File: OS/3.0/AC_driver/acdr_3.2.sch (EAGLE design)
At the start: 61 parts, among them T1 BT1308W, T2 MAC97SOT223, T3 MAC97SOT223, T4 MAC97SOT223, T5 MAC97SOT223, T6 MAC97SOT223, T7 MAC97SOT223, T8 MAC97SOT223

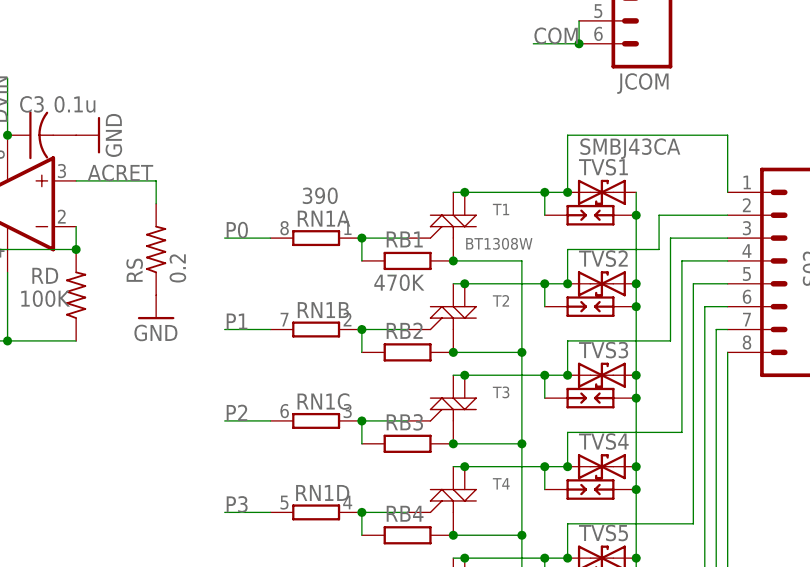
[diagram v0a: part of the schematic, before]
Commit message: correct the pull down resistor value
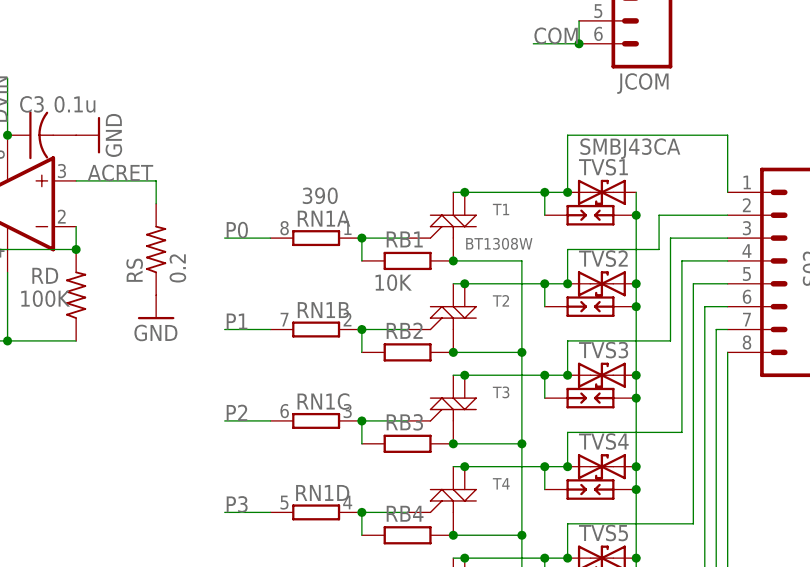
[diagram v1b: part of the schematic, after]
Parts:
- RB1, RB2, RB3, RB4, RB5, RB6, RB7, RB8: value 470K -> 10K
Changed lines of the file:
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@@
 <?xml version="1.0" encoding="utf-8"?>
 <!DOCTYPE eagle SYSTEM "eagle.dtd">
-<eagle version="9.3.0">
+<eagle version="9.6.2">
 <drawing>
 <settings>
@@
 <part name="SP7" library="varistor" deviceset="PCB-SGAP" device="" value="PCB-SGAP"/>
 <part name="SP8" library="varistor" deviceset="PCB-SGAP" device="" value="PCB-SGAP"/>
-<part name="RB1" library="rcl" deviceset="R-EU_" device="R0603" value="470K"/>
-<part name="RB2" library="rcl" deviceset="R-EU_" device="R0603" value="470K"/>
-<part name="RB3" library="rcl" deviceset="R-EU_" device="R0603" value="470K"/>
-<part name="RB4" library="rcl" deviceset="R-EU_" device="R0603" value="470K"/>
-<part name="RB5" library="rcl" deviceset="R-EU_" device="R0603" value="470K"/>
-<part name="RB6" library="rcl" deviceset="R-EU_" device="R0603" value="470K"/>
-<part name="RB7" library="rcl" deviceset="R-EU_" device="R0603" value="470K"/>
-<part name="RB8" library="rcl" deviceset="R-EU_" device="R0603" value="470K"/>
+<part name="RB1" library="rcl" deviceset="R-EU_" device="R0603" value="10K"/>
+<part name="RB2" library="rcl" deviceset="R-EU_" device="R0603" value="10K"/>
+<part name="RB3" library="rcl" deviceset="R-EU_" device="R0603" value="10K"/>
+<part name="RB4" library="rcl" deviceset="R-EU_" device="R0603" value="10K"/>
+<part name="RB5" library="rcl" deviceset="R-EU_" device="R0603" value="10K"/>
+<part name="RB6" library="rcl" deviceset="R-EU_" device="R0603" value="10K"/>
+<part name="RB7" library="rcl" deviceset="R-EU_" device="R0603" value="10K"/>
+<part name="RB8" library="rcl" deviceset="R-EU_" device="R0603" value="10K"/>
 <part name="SP0" library="varistor" deviceset="PCB-SGAP" device="" value="PCB-SGAP"/>
 <part name="GND1" library="SparkFun" deviceset="GND" device=""/>
